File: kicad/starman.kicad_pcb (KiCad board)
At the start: 4 copper layers, 182 x 150 mm, 207 parts, among them J1 M20-8771246, J10 Barrel_Jack_MountingPin, J11 Conn_02x01, J2 M20-8771246, J3 M20-8771246, J4 ESW-106-44-T-S, J5 Conn_02x03_Counter_Clockwise, J6 ESW-112-44-T-S, J7 Conn_01x10, J8 ESW-112-44-T-S, J9 Conn_01x10, SW1 SW_SPST, SW2 SW_SPST, U1 ESP32-S2-MINI-1, U2 PCA9959, U3 PCA9959, U4 PCA9959, U5 PCA9959, U6 PCA9959, U7 PCA9959, U8 NCP59301, U9 LF33, Y1 20Mhz, Y2 20Mhz, Y3 20Mhz, Y4 20Mhz, Y5 20Mhz, Y6 20Mhz

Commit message: Set mask clearance to 0.22mm
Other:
- rule pad_to_mask_clearance: 0.25 -> 0.22
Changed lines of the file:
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@@
       (dielectric_constraints no)
     )
-    (pad_to_mask_clearance 0.25)
+    (pad_to_mask_clearance 0.22)
     (grid_origin 30 180)
     (pcbplotparams
@@
     (fp_line (start 1 -0.625) (end 1 0.625) (layer "F.Fab") (width 0.1))
     (fp_line (start -1 0.625) (end -1 -0.625) (layer "F.Fab") (width 0.1))
-    (pad "1" smd roundrect (at -0.9125 0) (size 1.025 1.4) (layers "F.Cu" "F.Paste" "F.Mask") (roundrect_rratio 0.243902)
+    (pad "1" smd roundrect (at -0.9125 0) (size 1.025 1.4) (layers "F.Cu" "F.Paste" "F.Mask") (roundrect_rratio 0.243902439)
       (net 262 "Net-(R1-Pad1)") (pintype "passive"))
-    (pad "2" smd roundrect (at 0.9125 0) (size 1.025 1.4) (layers "F.Cu" "F.Paste" "F.Mask") (roundrect_rratio 0.243902)
+    (pad "2" smd roundrect (at 0.9125 0) (size 1.025 1.4) (layers "F.Cu" "F.Paste" "F.Mask") (roundrect_rratio 0.243902439)
       (net 4 "+5V") (pintype "passive"))
     (model "${KICAD6_3DMODEL_DIR}/Resistor_SMD.3dshapes/R_0805_2012Metric.wrl"

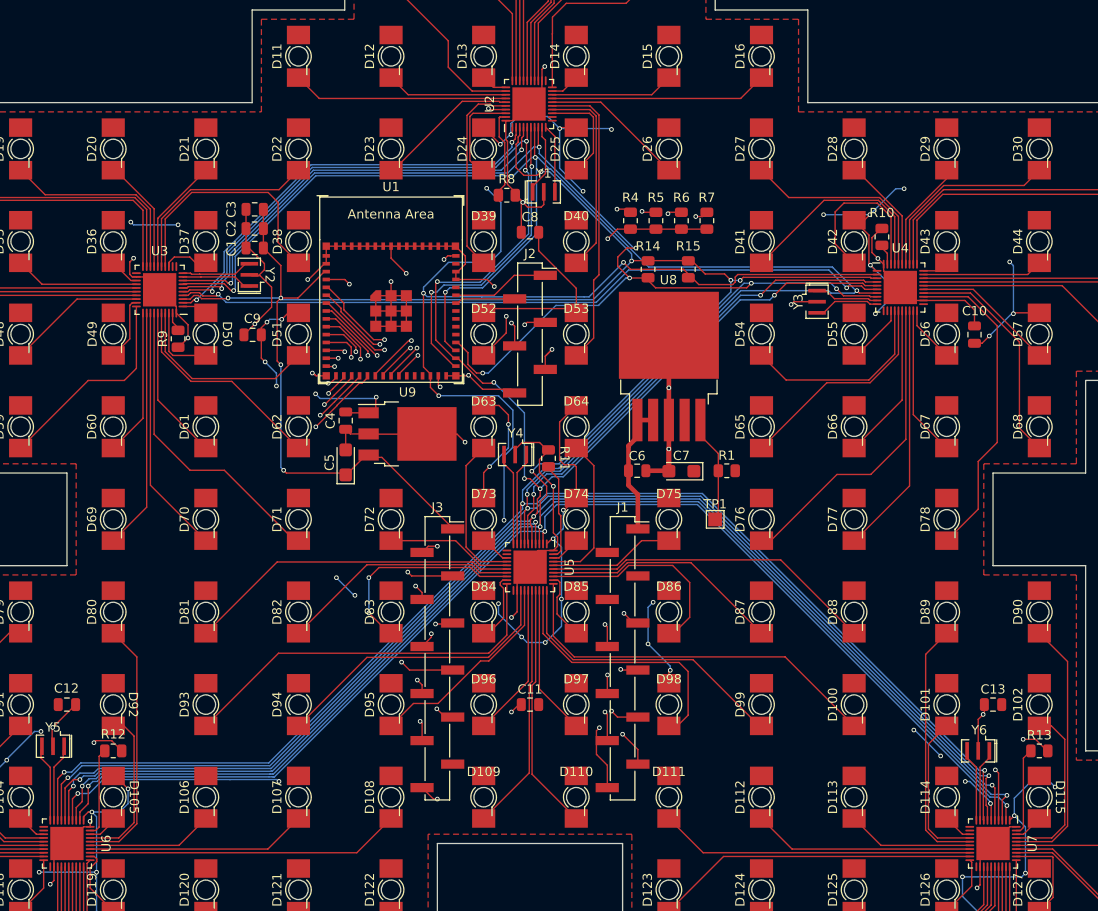
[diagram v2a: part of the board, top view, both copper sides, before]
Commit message: Run DRC, correct for spacing -- Fixed +5V to C11, D97, D110
WARNING: there is a risk that C11 and D97 and D110 are not connected to
+5V as this design already went for production.  A bodge wire may be needed.

At least its fixed for any future builds
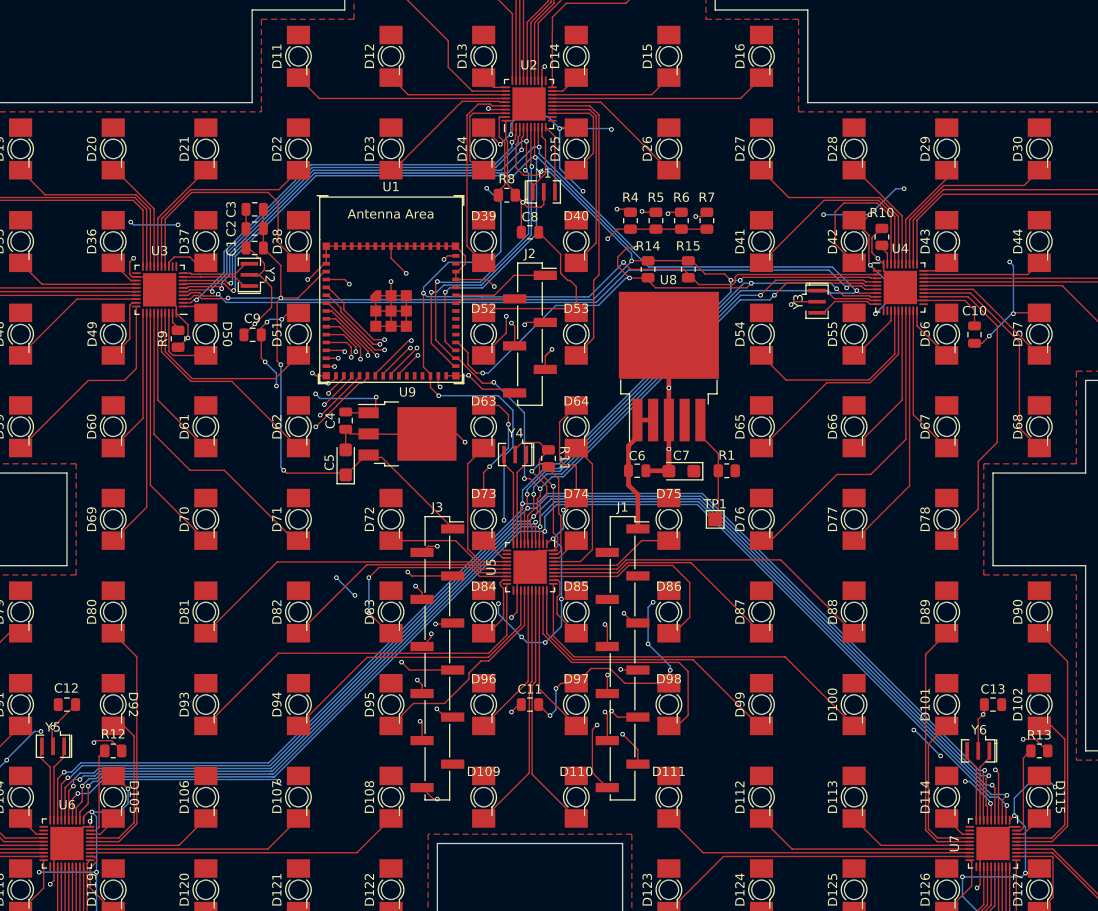
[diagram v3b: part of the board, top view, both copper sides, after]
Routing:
- net /GPIO8: track 0.00 -> 62.4 mm, vias 0 -> 2
- net /GPIO6: track 120.3 -> 58.1 mm, vias 4 -> 2
- net +5V: track 259.4 -> 278.2 mm, vias 50 -> 52

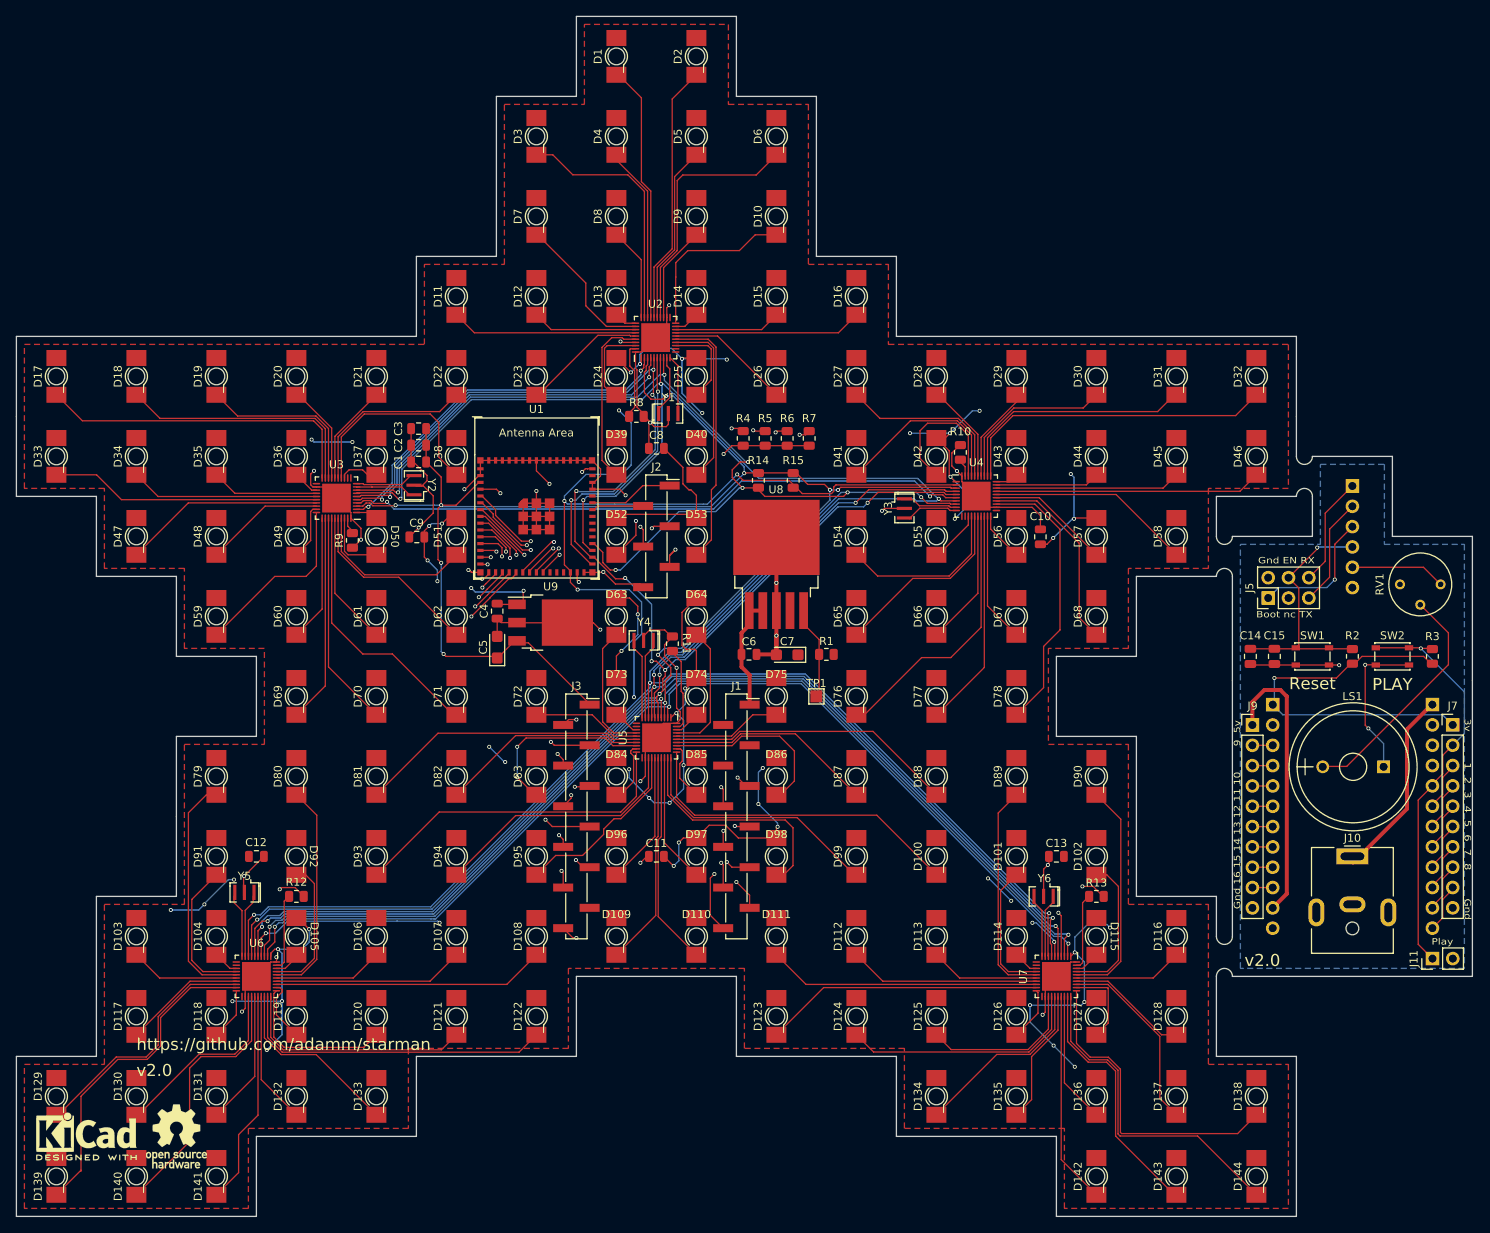
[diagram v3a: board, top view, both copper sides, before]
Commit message: Reduce footprint and margins of OSRAM P47F LED
Will be required to allow for space for the NXP chip replacement
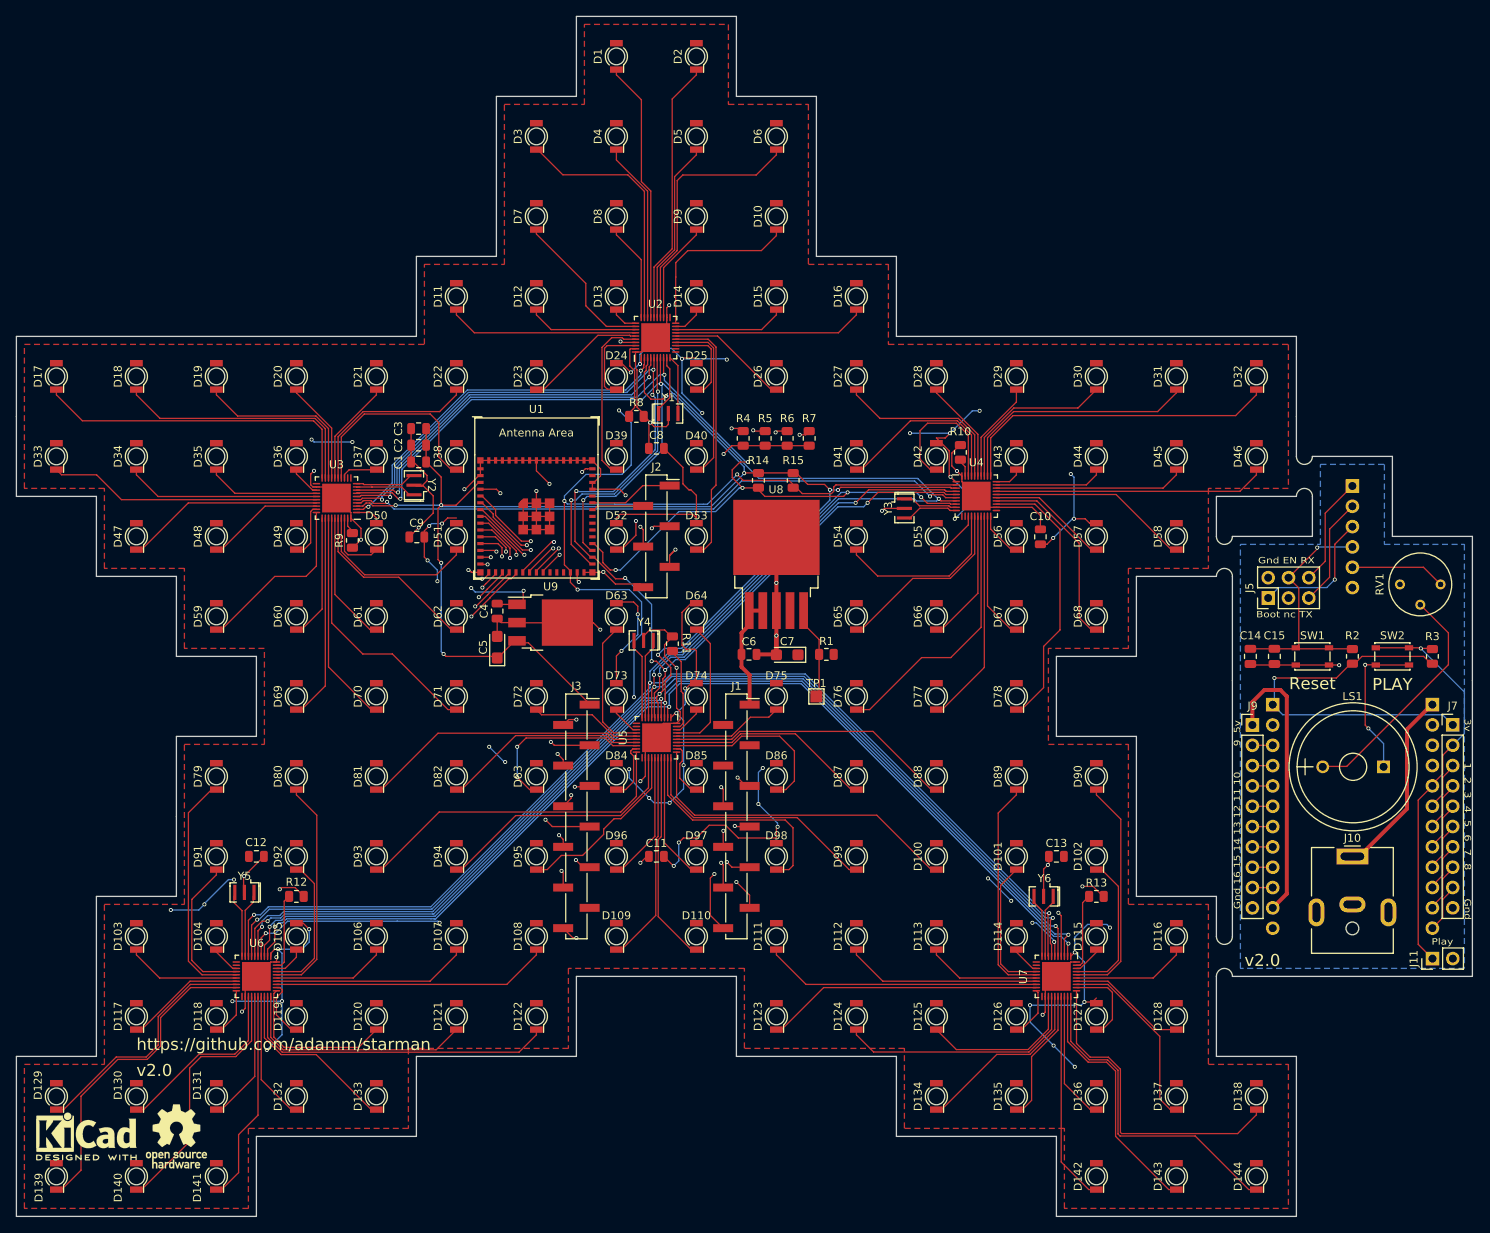
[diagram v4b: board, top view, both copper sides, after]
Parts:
- D1, D10, D100, D101, D102, D103, D104, D105, D106, D107, D108, D109, D11, D110, D111, D112, D113, D114, D115, D116, D117, D118, D119, D12, D120, D121, D122, D123, D124, D125, D126, D127, D128, D129, D13, D130, D131, D132, D133, D134, D135, D136, D137, D138, D139, D14, D140, D141, D142, D143, D144, D15, D16, D17, D18, D19, D2, D20, D21, D22, D23, D24, D25, D26, D27, D28, D29, D3, D30, D31, D32, D33, D34, D35, D36, D37, D38, D39, D4, D40, D41, D42, D43, D44, D45, D46, D47, D48, D49, D5, D50, D51, D52, D53, D54, D55, D56, D57, D58, D59, D6, D60, D61, D62, D63, D64, D65, D66, D67, D68, D69, D7, D70, D71, D72, D73, D74, D75, D76, D77, D78, D79, D8, D80, D81, D82, D83, D84, D85, D86, D87, D88, D89, D9, D90, D91, D92, D93, D94, D95, D96, D97, D98, D99: footprint LED_SMD:LED_Osram_Lx_P47F_D2mm_ReverseMount -> starman:LED_Osram_Lx_P47F_D2mm_ReverseMount
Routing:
- net +5V: track 278.2 -> 279.4 mm
- net Net-(D10-Pad1): track 21.6 -> 22.3 mm
- net Net-(D91-Pad1): track 18.1 -> 18.8 mm
- net Net-(D138-Pad1): track 39.3 -> 40.0 mm
- net Net-(D124-Pad1): track 30.6 -> 31.2 mm
- net Net-(D122-Pad1): track 40.4 -> 41.0 mm
- net Net-(D116-Pad1): track 13.7 -> 14.3 mm
- net Net-(D113-Pad1): track 13.7 -> 14.3 mm
- net Net-(D112-Pad1): track 23.9 -> 24.5 mm
- net Net-(D111-Pad1): track 34.0 -> 34.7 mm
- net Net-(D108-Pad1): track 34.0 -> 34.7 mm
- net Net-(D107-Pad1): track 23.9 -> 24.5 mm
- net Net-(D106-Pad1): track 13.7 -> 14.3 mm
- net Net-(D105-Pad1): track 3.37 -> 4.02 mm
- net Net-(D103-Pad1): track 13.7 -> 14.3 mm
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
